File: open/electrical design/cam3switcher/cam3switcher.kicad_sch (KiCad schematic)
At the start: 2 parts, among them J1 DSI, J2 DSI

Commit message: minor changes to switcher board
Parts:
- J1: footprint (none) -> Connector_FFC-FPC:TE_1-84952-5_1x15-1MP_P1.0mm_Horizontal
- J2: value DSI -> CSI; footprint (none) -> Connector_FFC-FPC:TE_1-84952-5_1x15-1MP_P1.0mm_Horizontal
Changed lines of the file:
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@@
       (effects (font (size 1.27 1.27)))
     )
-    (property "Footprint" "" (at 45.72 55.88 0)
+    (property "Footprint" "Connector_FFC-FPC:TE_1-84952-5_1x15-1MP_P1.0mm_Horizontal" (at 45.72 55.88 0)
       (effects (font (size 1.27 1.27)) hide)
     )
@@
   (symbol (lib_id "power:+3V3") (at 57.15 76.2 180) (unit 1)
     (in_bom yes) (on_board yes) (dnp no) (fields_autoplaced)
-    (property "Reference" "#PWR02" (at 57.15 72.39 0)
+    (property "Reference" "#PWR01" (at 57.15 72.39 0)
       (effects (font (size 1.27 1.27)) hide)
     )
@@
       (project "cam3switcher"
         (path "/48668e53-5170-44d6-b6a2-f39b59615f11"
-          (reference "#PWR02") (unit 1)
+          (reference "#PWR01") (unit 1)
         )
       )
@@
       (effects (font (size 1.27 1.27)) (justify right))
     )
-    (property "Value" "DSI" (at 80.01 35.56 0)
+    (property "Value" "CSI" (at 80.01 35.56 0)
       (effects (font (size 1.27 1.27)) (justify right))
     )
-    (property "Footprint" "" (at 81.28 55.88 0)
+    (property "Footprint" "Connector_FFC-FPC:TE_1-84952-5_1x15-1MP_P1.0mm_Horizontal" (at 81.28 55.88 0)
       (effects (font (size 1.27 1.27)) hide)
     )
@@
   (symbol (lib_id "power:GND") (at 63.5 76.2 0) (unit 1)
     (in_bom yes) (on_board yes) (dnp no) (fields_autoplaced)
-    (property "Reference" "#PWR01" (at 63.5 82.55 0)
+    (property "Reference" "#PWR02" (at 63.5 82.55 0)
       (effects (font (size 1.27 1.27)) hide)
     )
@@
       (project "cam3switcher"
         (path "/48668e53-5170-44d6-b6a2-f39b59615f11"
-          (reference "#PWR01") (unit 1)
+          (reference "#PWR02") (unit 1)
         )
       )

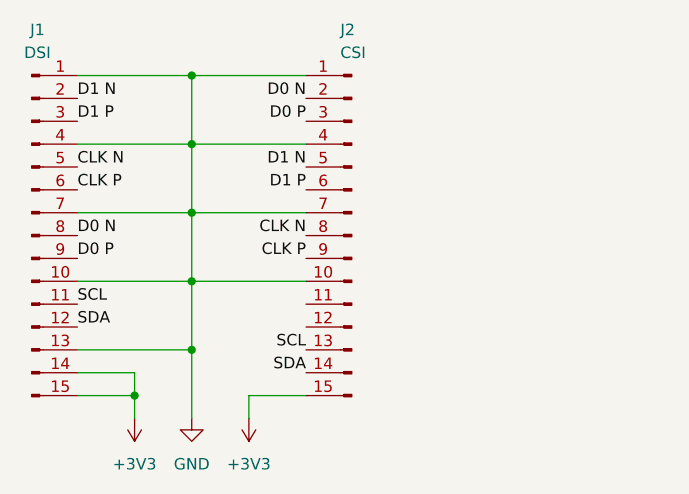
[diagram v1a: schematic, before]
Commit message: switcher board router i2c of camera to csi i2c lanes
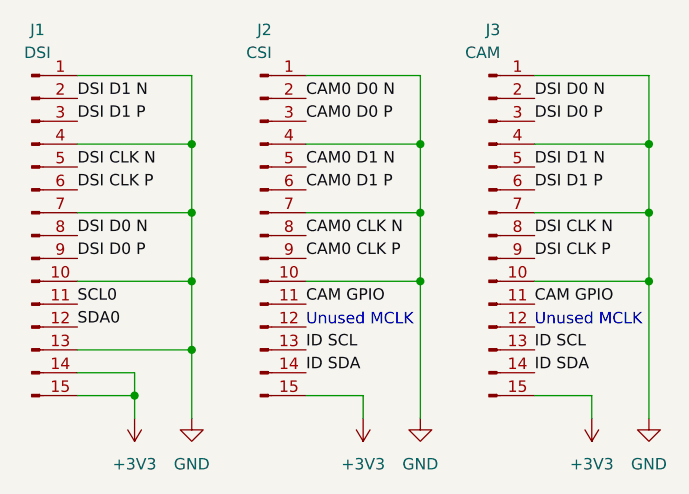
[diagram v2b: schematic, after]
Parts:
- added J2: CSI, Connector_FFC-FPC:TE_1-84952-5_1x15-1MP_P1.0mm_Horizontal, symbol Connector:Conn_01x15_Pin
- J3: renamed from J2; value CSI -> CAM
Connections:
- net +3V3: now also J2.15 (Pin_15)
- net GND: now also J2.1 (Pin_1), J2.10 (Pin_10), J2.4 (Pin_4), J2.7 (Pin_7)
- net CAM GPIO: now reaches J3.11 (Pin_11)
- net CAM GPIO: now also J2.11 (Pin_11)
- net CLK N renamed DSI CLK N
- net CLK P renamed DSI CLK P
- net D0 N renamed DSI D0 N
- net D0 P renamed DSI D0 P
- net D1 N renamed DSI D1 N
- net D1 P renamed DSI D1 P
- net SCL renamed ID SCL
- net ID SCL: now also J2.13 (Pin_13); no longer J1.11 (Pin_11)
- net SDA renamed ID SDA
- net ID SDA: now also J2.14 (Pin_14); no longer J1.12 (Pin_12)
- new net CAM0 CLK N: J2.8 (Pin_8)
- new net CAM0 CLK P: J2.9 (Pin_9)
- new net CAM0 D0 N: J2.2 (Pin_2)
- new net CAM0 D0 P: J2.3 (Pin_3)
- new net CAM0 D1 N: J2.5 (Pin_5)
- new net CAM0 D1 P: J2.6 (Pin_6)
- new net SCL0: J1.11 (Pin_11)
- new net SDA0: J1.12 (Pin_12)
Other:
- note added: "Unused MCLK"
- moved on the sheet: J3
